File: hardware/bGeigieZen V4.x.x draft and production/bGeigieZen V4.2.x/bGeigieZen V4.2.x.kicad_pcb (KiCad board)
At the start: 2 copper layers, 129.4 x 64.6 mm, 13 parts, among them J1 M5 2x15 pin, J3 GPS, J4 Geiger Safepulse, J5 Extra support header

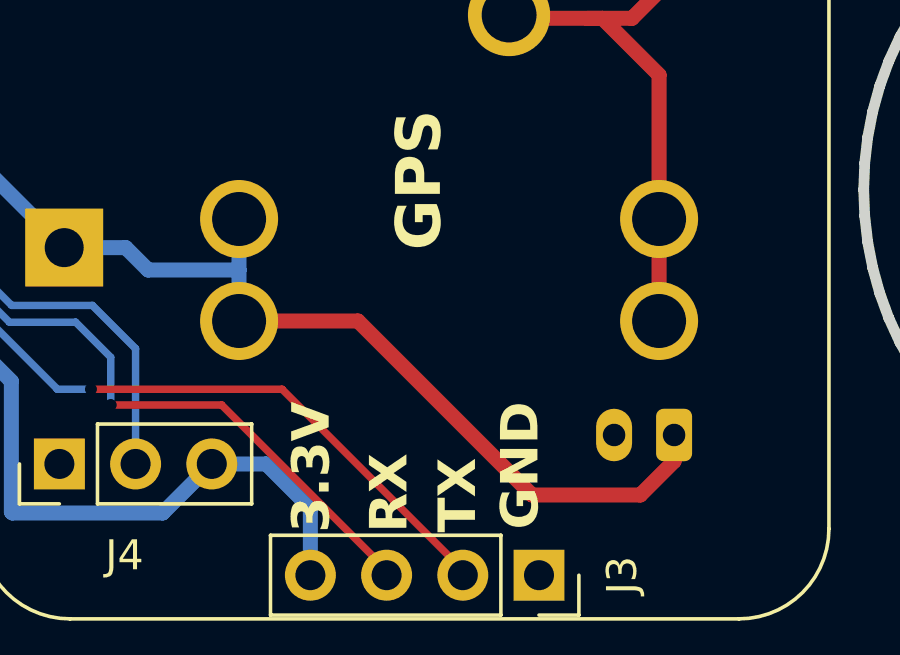
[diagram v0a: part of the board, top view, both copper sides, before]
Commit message: fix: enable deadtime correction in log header and adjust PCB component positions
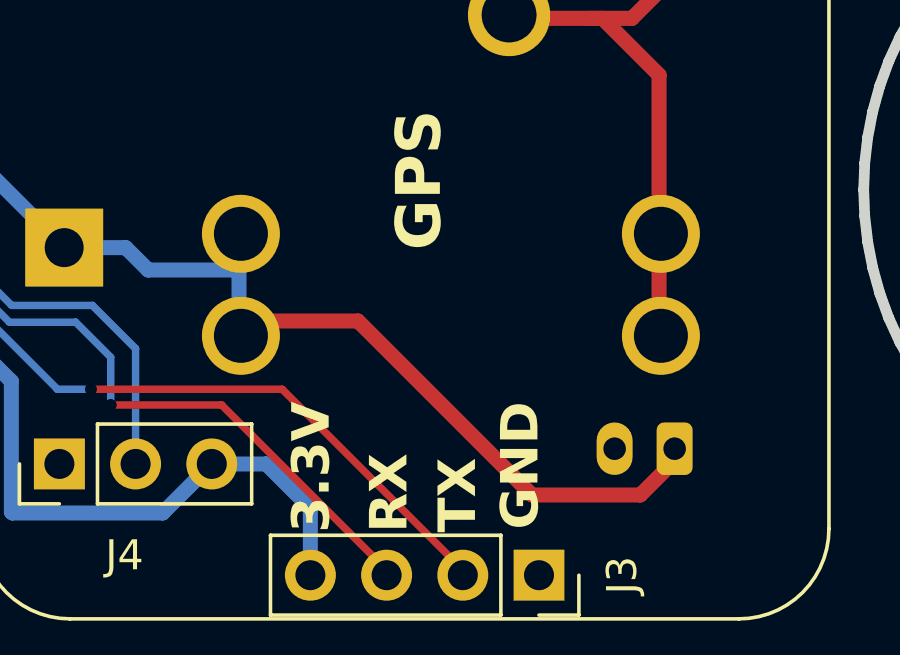
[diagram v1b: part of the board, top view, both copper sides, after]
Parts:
- moved Fuse 2A 0.50 mm to (197.4, 89.0)
- moved QI-charger 0.46 mm to (204.8, 94.5)
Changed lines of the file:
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@@
 	(footprint "bGeigieZen:FUSE_3557-2"
 		(layer "B.Cu")
-		(at 197.3076 88.53 180)
+		(at 197.3684 89.024 180)
 		(property "Reference" "Fuse 2A"
 			(at -11.5 0.5 90)
@@
 	(footprint "Connector_JST:JST_PH_B2B-PH-K_1x02_P2.00mm_Vertical"
 		(layer "B.Cu")
-		(at 204.8076 94.03 180)
+		(at 204.8256 94.4868 180)
 		(descr "JST PH series connector, B2B-PH-K (http://www.jst-mfg.com/product/pdf/eng/ePH.pdf), generated with kicad-footprint-generator")
 		(tags "connector JST PH side entry")

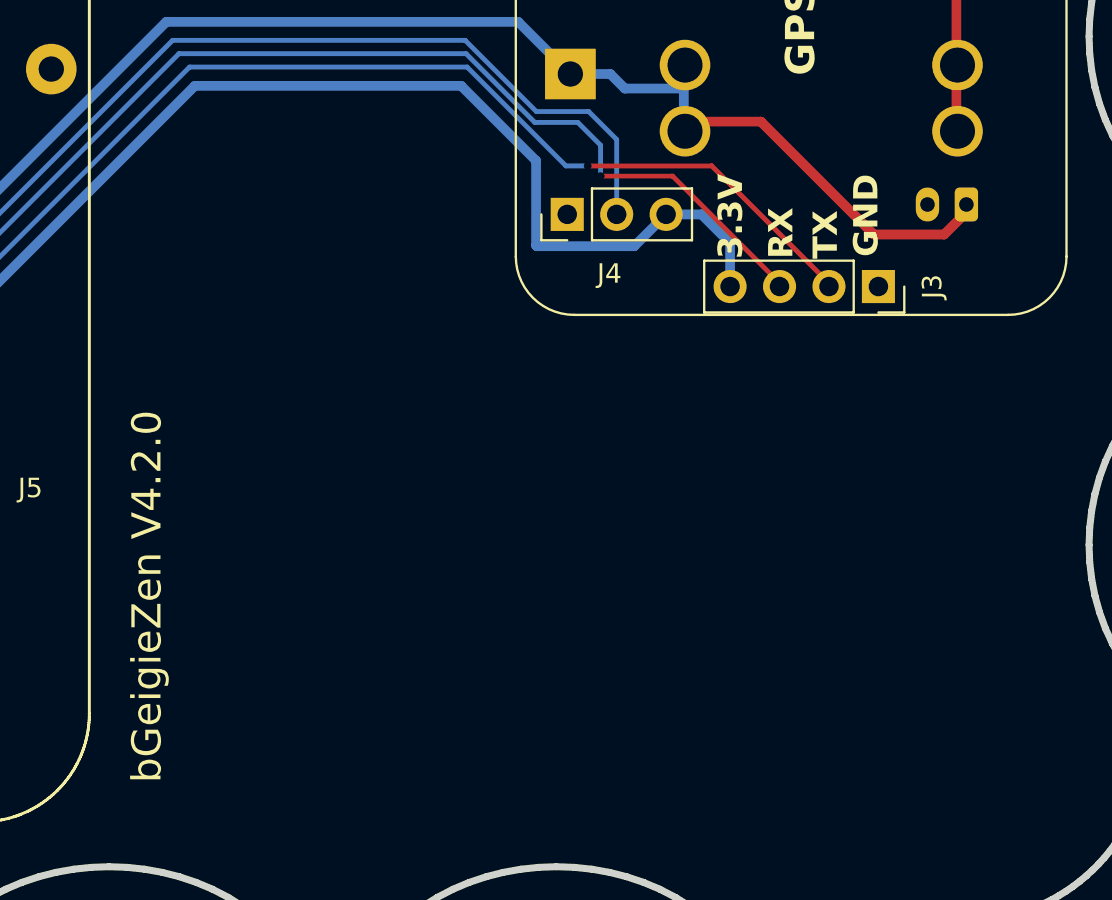
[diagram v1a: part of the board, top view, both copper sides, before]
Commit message: feat: update PCB version to V4.2.1 and adjust QI charger connector position
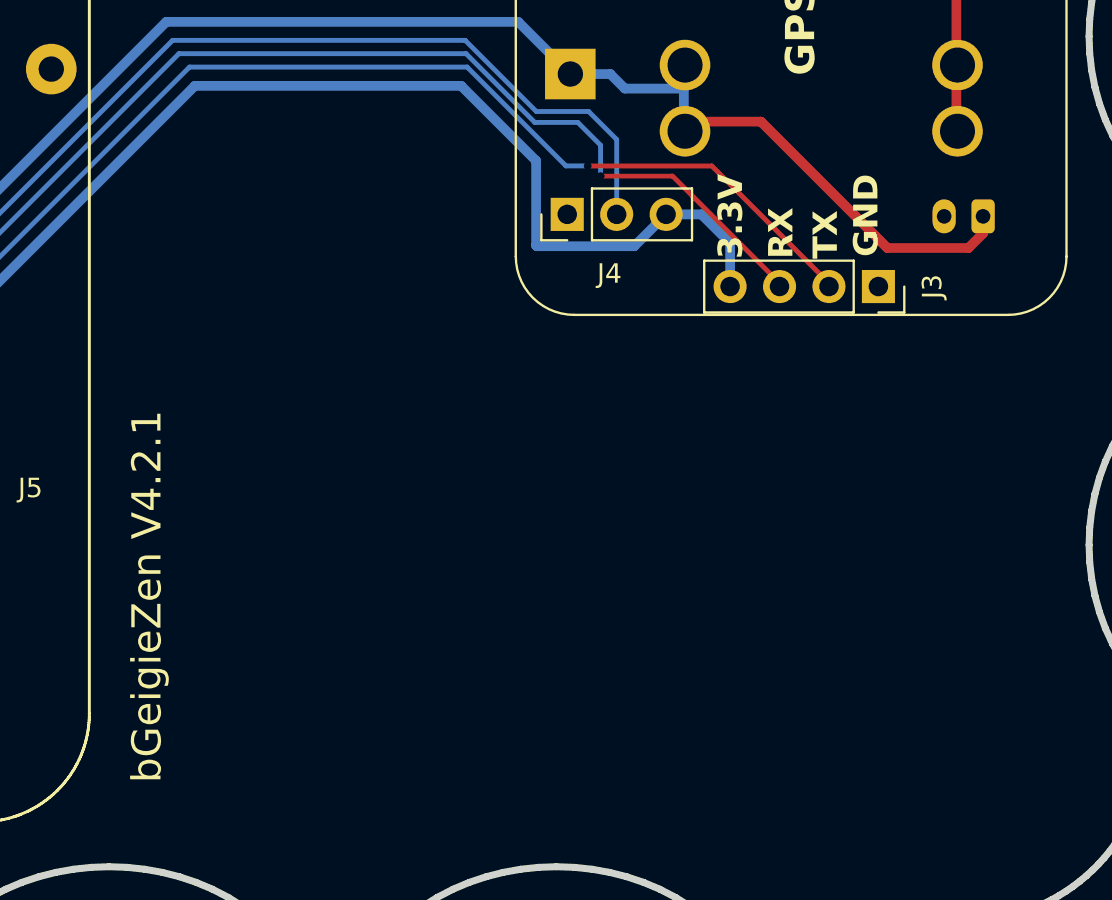
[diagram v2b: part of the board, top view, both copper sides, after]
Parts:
- moved QI-charger 1.05 mm to (205.7, 95.1)
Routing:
- net /BAT: track 111.3 -> 112.3 mm
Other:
- board text added: "bGeigieZen V4.2.1"
- board text removed: "bGeigieZen V4.2.0"
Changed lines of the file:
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@@
 	(paper "A4")
 	(title_block
-		(title "bGeigieZenV4.2.0")
-		(date "2025-07-19")
-		(rev "V4.2.0")
+		(title "bGeigieZenV4.2.1")
+		(date "2025-10-10")
+		(rev "V4.2.1")
 		(comment 1 "New standant")
 	)
@@
 	(footprint "Connector_JST:JST_PH_B2B-PH-K_1x02_P2.00mm_Vertical"
 		(layer "B.Cu")
-		(at 204.8256 94.4868 180)
+		(at 205.6826 95.0964 180)
 		(descr "JST PH series connector, B2B-PH-K (http://www.jst-mfg.com/product/pdf/eng/ePH.pdf), generated with kicad-footprint-generator")
 		(tags "connector JST PH side entry")
@@
 		)
 	)
-	(gr_text "bGeigieZen V4.2.0\n\n"
+	(gr_text "bGeigieZen V4.2.1\n\n"
 		(at 163.9316 124.2048 90)
 		(layer "F.SilkS")
@@
 		)
 	)
-	(gr_text "bGeigieZen V4.2.0\n\n"
+	(gr_text "bGeigieZen V4.2.1\n\n"
 		(at 201.422 106.2216 90)
 		(layer "B.SilkS")
@@
 	)
 	(segment
-		(start 203.6826 96.03)
-		(end 200.070342 96.03)
+		(start 194.270342 90.23)
+		(end 200.762742 96.7224)
 		(width 0.5)
 		(layer "F.Cu")
@@
 	)
 	(segment
-		(start 194.270342 90.23)
-		(end 190.3076 90.23)
+		(start 205.6826 95.9714)
+		(end 205.6826 95.0964)
 		(width 0.5)
 		(layer "F.Cu")
@@
 	)
 	(segment
-		(start 200.070342 96.03)
-		(end 194.270342 90.23)
+		(start 204.9316 96.7224)
+		(end 205.6826 95.9714)
 		(width 0.5)
 		(layer "F.Cu")
@@
 	)
 	(segment
-		(start 204.8076 94.03)
-		(end 204.8076 94.905)
+		(start 190.3076 90.23)
+		(end 194.270342 90.23)
 		(width 0.5)
 		(layer "F.Cu")
@@
 	)
 	(segment
-		(start 204.8076 94.905)
-		(end 203.6826 96.03)
+		(start 200.762742 96.7224)
+		(end 204.9316 96.7224)
 		(width 0.5)
 		(layer "F.Cu")
